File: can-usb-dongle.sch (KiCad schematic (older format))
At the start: 43 parts, among them SW1 SW_PUSH, U1 STM32F302C8T, U2 SN65HVD256, U3 NUF2042XV6, U4 MCP1700, U5 SiP32431, X1 16MHz 10ppm

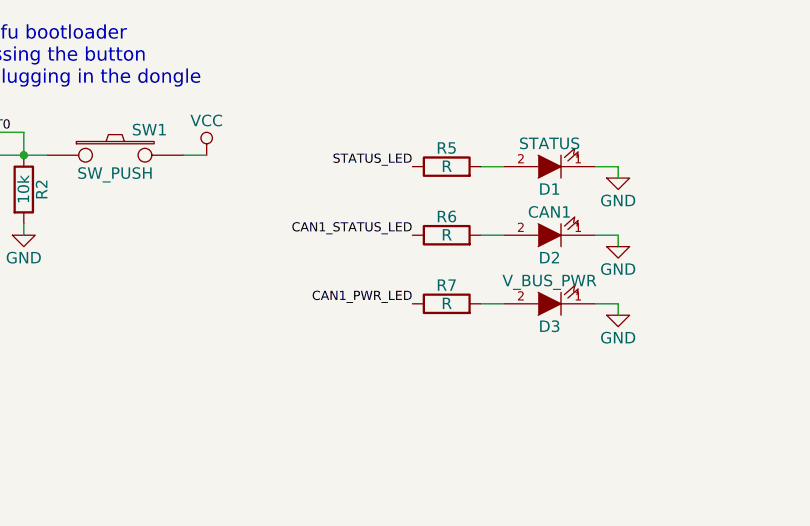
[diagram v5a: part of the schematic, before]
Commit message: Update LED resistor values.
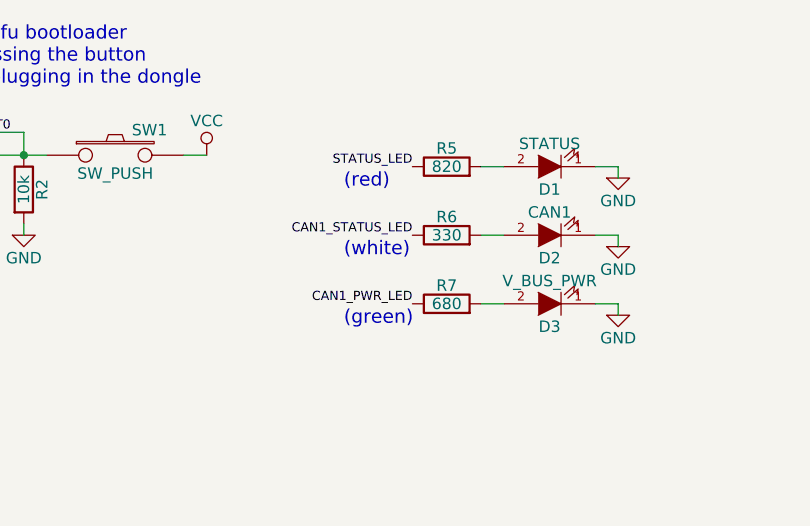
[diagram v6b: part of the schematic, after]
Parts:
- R5: value R -> 820
- R6: value R -> 330
- R7: value R -> 680
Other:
- note added: "(green)"
- note added: "(red)"
- note added: "(white)"
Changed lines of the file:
@@
 P 6150 1750
 F 0 "R6" V 6230 1750 50  0000 C CNN
-F 1 "R" V 6150 1750 50  0000 C CNN
+F 1 "330" V 6150 1750 50  0000 C CNN
 F 2 "_std:_0603" V 6080 1750 30  0001 C CNN
 F 3 "" H 6150 1750 30  0000 C CNN
@@
 P 6150 1450
 F 0 "R5" V 6230 1450 50  0000 C CNN
-F 1 "R" V 6150 1450 50  0000 C CNN
+F 1 "820" V 6150 1450 50  0000 C CNN
 F 2 "_std:_0603" V 6080 1450 30  0001 C CNN
 F 3 "" H 6150 1450 30  0000 C CNN
@@
 P 6150 2050
 F 0 "R7" V 6230 2050 50  0000 C CNN
-F 1 "R" V 6150 2050 50  0000 C CNN
+F 1 "680" V 6150 2050 50  0000 C CNN
 F 2 "_std:_0603" V 6080 2050 30  0001 C CNN
 F 3 "" H 6150 2050 30  0000 C CNN
@@
 	1    0    0    -1
 $EndComp
+Text Notes 5700 1550 0    60   ~ 0
+(red)
+Text Notes 5700 1850 0    60   ~ 0
+(white)
+Text Notes 5700 2150 0    60   ~ 0
+(green)
 $EndSCHEMATC

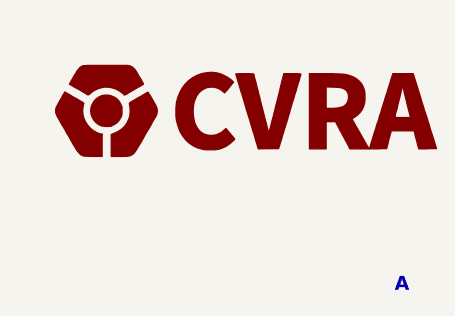
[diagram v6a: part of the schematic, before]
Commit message: Start RevB, add missing STATUS LED track
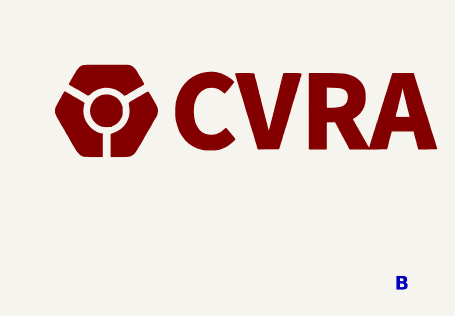
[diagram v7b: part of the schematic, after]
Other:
- note added: "B"
- note removed: "A"
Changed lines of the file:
@@
 CAN to USB adapter dongle
 Text Notes 10750 7650 0    60   ~ 12
-A
+B
 Text Notes 8200 7650 0    60   ~ 0
 25.10.2015
